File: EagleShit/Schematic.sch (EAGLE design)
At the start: 4 parts

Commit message: New schematic with board!
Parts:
- added C1, C2: (no value), rcl:CPOL-EUE2,5-6E
- added MOTOR_1, MOTOR_2: (no value), con-lstb:MA04-1
- added U$3: XT60_XT60, XT60_LipoConnector:XT60_XT60
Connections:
- removed net GND: ARDUINO_NANO1.GND@1, U$1.GND, U$2.GND
- removed net N$4: ARDUINO_NANO1.GND@2, LORA1.GND
- removed net VCC: ARDUINO_NANO1.VIN, U$1.VMOT, U$2.VMOT
- new net GNDA: ARDUINO_NANO1.GND@1, C1.-, C2.-, LORA1.GND, U$1.GND, U$2.GND, U$3.GND
- new net N$11: ARDUINO_NANO1.VIN, C1.+, C2.+, U$1.VMOT, U$2.VMOT, U$3.VCC
- new net N$15: MOTOR_1.4, U$1.2B
- new net N$16: MOTOR_1.3, U$1.2A
- new net N$17: MOTOR_1.2, U$1.1A
- new net N$18: MOTOR_1.1, U$1.1B
- new net N$19: MOTOR_2.4, U$2.2B
- new net N$20: MOTOR_2.3, U$2.2A
- new net N$21: MOTOR_2.2, U$2.1A
- new net N$22: MOTOR_2.1, U$2.1B

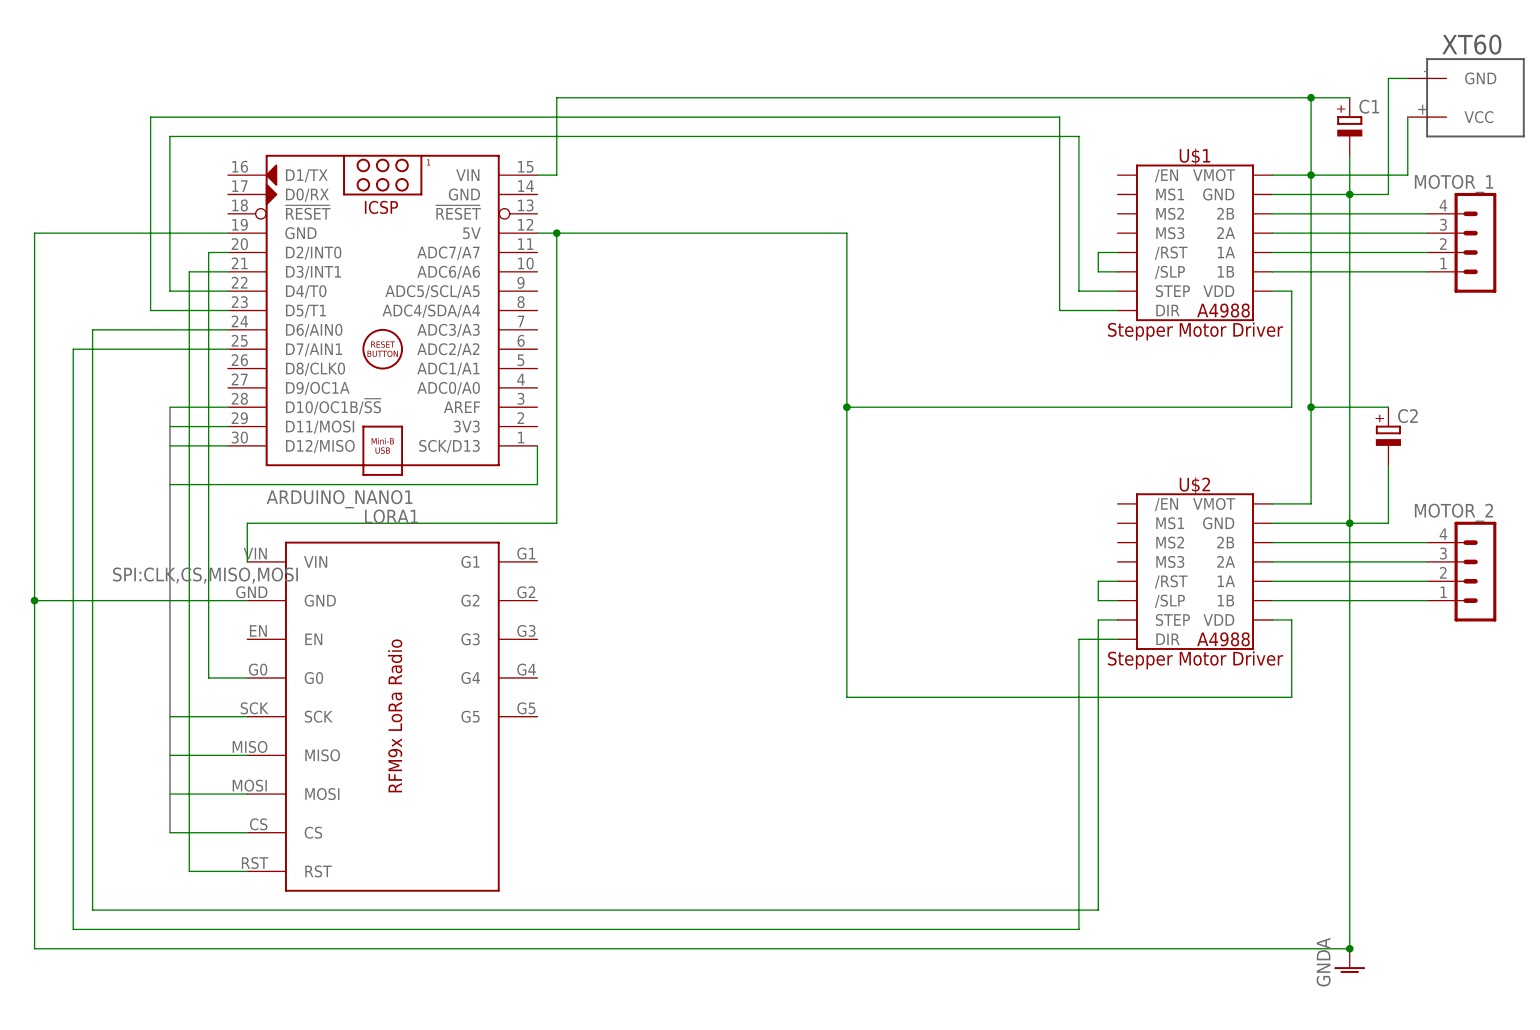
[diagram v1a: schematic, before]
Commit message: Added Enable Pins
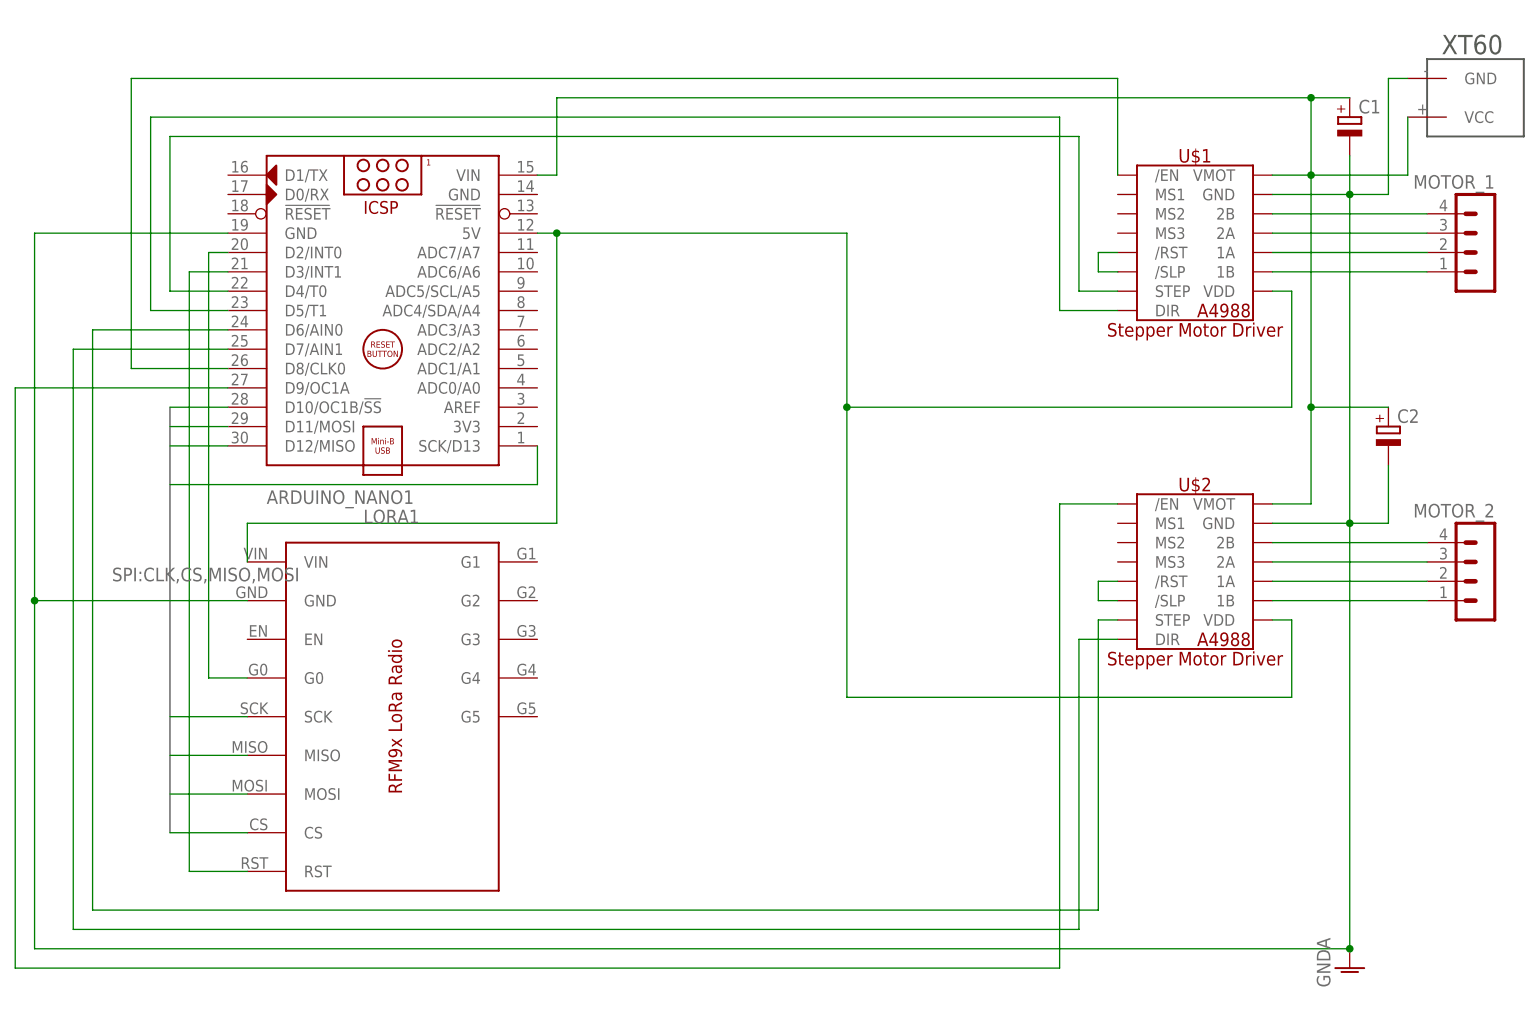
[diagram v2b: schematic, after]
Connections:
- new net N$12: ARDUINO_NANO1.D9/OC1A, U$2./EN
- new net N$4: ARDUINO_NANO1.D8/CLK0, U$1./EN
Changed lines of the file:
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@@
+</segment>
+</net>
+<net name="N$4" class="0">
+<segment>
+<pinref part="ARDUINO_NANO1" gate="G$1" pin="D8/CLK0"/>
+<wire x1="5.08" y1="63.5" x2="-7.62" y2="63.5" width="0.1524" layer="91"/>
+<wire x1="-7.62" y1="63.5" x2="-7.62" y2="101.6" width="0.1524" layer="91"/>
+<wire x1="-7.62" y1="101.6" x2="121.92" y2="101.6" width="0.1524" layer="91"/>
+<pinref part="U$1" gate="G$1" pin="/EN"/>
+<wire x1="121.92" y1="101.6" x2="121.92" y2="88.9" width="0.1524" layer="91"/>
+</segment>
+</net>
+<net name="N$12" class="0">
+<segment>
+<pinref part="ARDUINO_NANO1" gate="G$1" pin="D9/OC1A"/>
+<wire x1="5.08" y1="60.96" x2="-22.86" y2="60.96" width="0.1524" layer="91"/>
+<wire x1="-22.86" y1="60.96" x2="-22.86" y2="-15.24" width="0.1524" layer="91"/>
+<wire x1="-22.86" y1="-15.24" x2="114.3" y2="-15.24" width="0.1524" layer="91"/>
+<wire x1="114.3" y1="-15.24" x2="114.3" y2="45.72" width="0.1524" layer="91"/>
+<pinref part="U$2" gate="G$1" pin="/EN"/>
+<wire x1="114.3" y1="45.72" x2="121.92" y2="45.72" width="0.1524" layer="91"/>
 </segment>
 </net>
